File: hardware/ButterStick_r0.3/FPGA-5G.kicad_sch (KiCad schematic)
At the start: 1 part, among them U2 ECP5UM5G_85_CABGA381

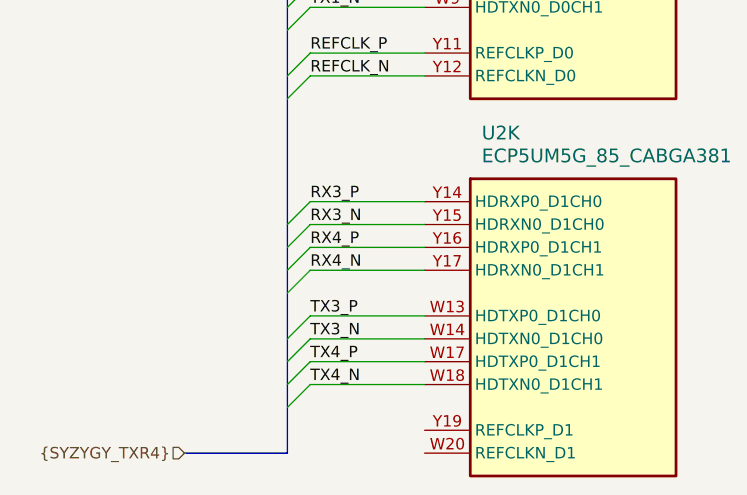
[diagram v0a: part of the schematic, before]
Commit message: hw.r0_3: routing improvements
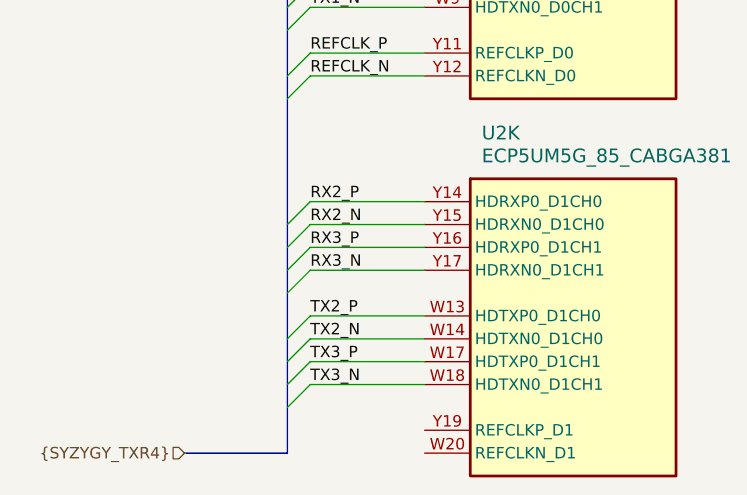
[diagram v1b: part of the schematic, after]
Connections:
- net RX4_N is gone; now on net RX3_N: U2.Y17 (HDRXN0_D1CH1)
- net RX4_P is gone; now on net RX3_P: U2.Y16 (HDRXP0_D1CH1)
- net TX4_N is gone; now on net TX3_N: U2.W18 (HDTXN0_D1CH1)
- net TX4_P is gone; now on net TX3_P: U2.W17 (HDTXP0_D1CH1)
- net RX3_N: no longer U2.Y15 (HDRXN0_D1CH0)
- net RX3_P: no longer U2.Y14 (HDRXP0_D1CH0)
- net TX3_N: no longer U2.W14 (HDTXN0_D1CH0)
- net TX3_P: no longer U2.W13 (HDTXP0_D1CH0)
- new net RX2_N: U2.Y15 (HDRXN0_D1CH0)
- new net RX2_P: U2.Y14 (HDRXP0_D1CH0)
- new net TX2_N: U2.W14 (HDTXN0_D1CH0)
- new net TX2_P: U2.W13 (HDTXP0_D1CH0)
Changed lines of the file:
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@@
 (kicad_sch (version 20200512) (host eeschema "5.99.0-unknown-c8476d6~101~ubuntu18.04.1")
-  (page 12 20)
+  (page 1 20)
   (paper "A4")
   (bus_entry (at 62.23 72.39) (size 2.54 -2.54))
@@
     (effects (font (size 1.27 1.27)) (justify left bottom))
   )
-  (label "RX3_P" (at 64.77 111.76 0)
+  (label "RX2_P" (at 64.77 111.76 0)
     (effects (font (size 1.27 1.27)) (justify left bottom))
   )
-  (label "RX3_N" (at 64.77 114.3 0)
+  (label "RX2_N" (at 64.77 114.3 0)
     (effects (font (size 1.27 1.27)) (justify left bottom))
   )
-  (label "RX4_P" (at 64.77 116.84 0)
+  (label "RX3_P" (at 64.77 116.84 0)
     (effects (font (size 1.27 1.27)) (justify left bottom))
   )
-  (label "RX4_N" (at 64.77 119.38 0)
+  (label "RX3_N" (at 64.77 119.38 0)
     (effects (font (size 1.27 1.27)) (justify left bottom))
   )
-  (label "TX3_P" (at 64.77 124.46 0)
+  (label "TX2_P" (at 64.77 124.46 0)
     (effects (font (size 1.27 1.27)) (justify left bottom))
   )
-  (label "TX3_N" (at 64.77 127 0)
+  (label "TX2_N" (at 64.77 127 0)
     (effects (font (size 1.27 1.27)) (justify left bottom))
   )
-  (label "TX4_P" (at 64.77 129.54 0)
+  (label "TX3_P" (at 64.77 129.54 0)
     (effects (font (size 1.27 1.27)) (justify left bottom))
   )
-  (label "TX4_N" (at 64.77 132.08 0)
+  (label "TX3_N" (at 64.77 132.08 0)
     (effects (font (size 1.27 1.27)) (justify left bottom))
   )

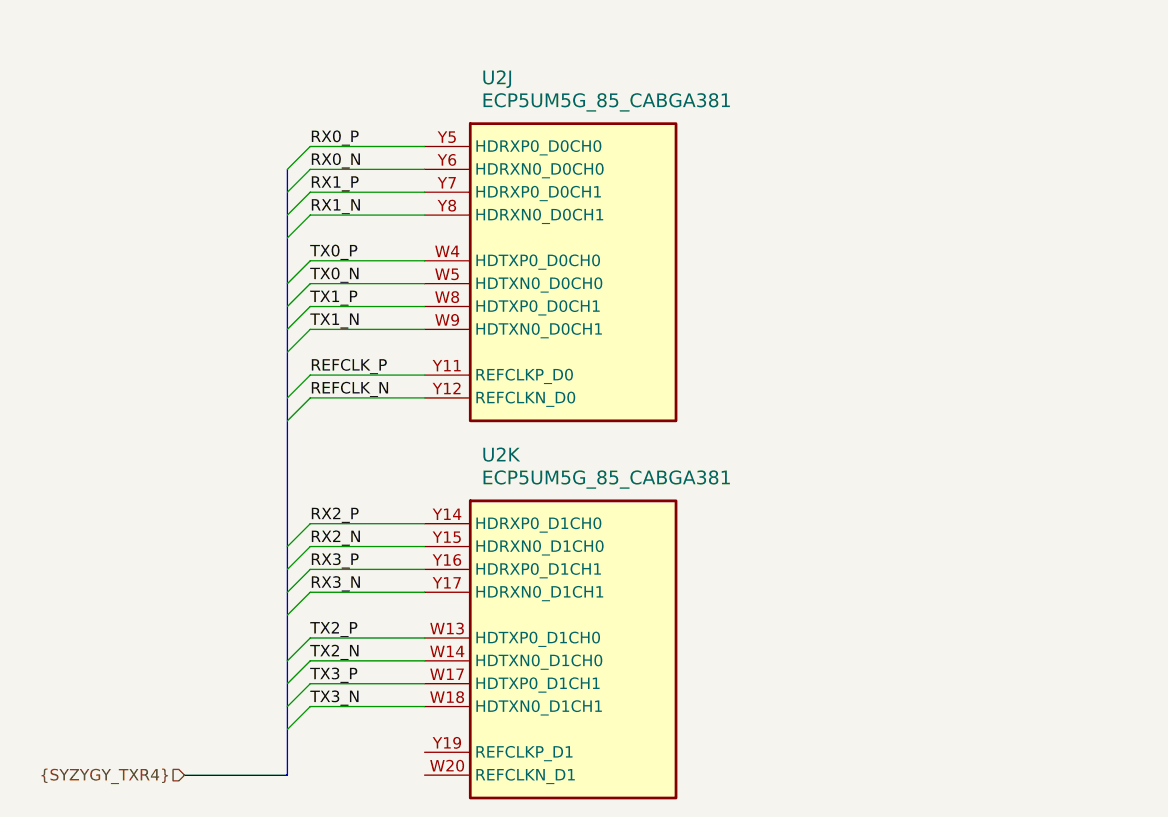
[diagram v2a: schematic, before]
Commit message: hw.r0_3: routed SYZYGY, begin routing RGMII/ULPI
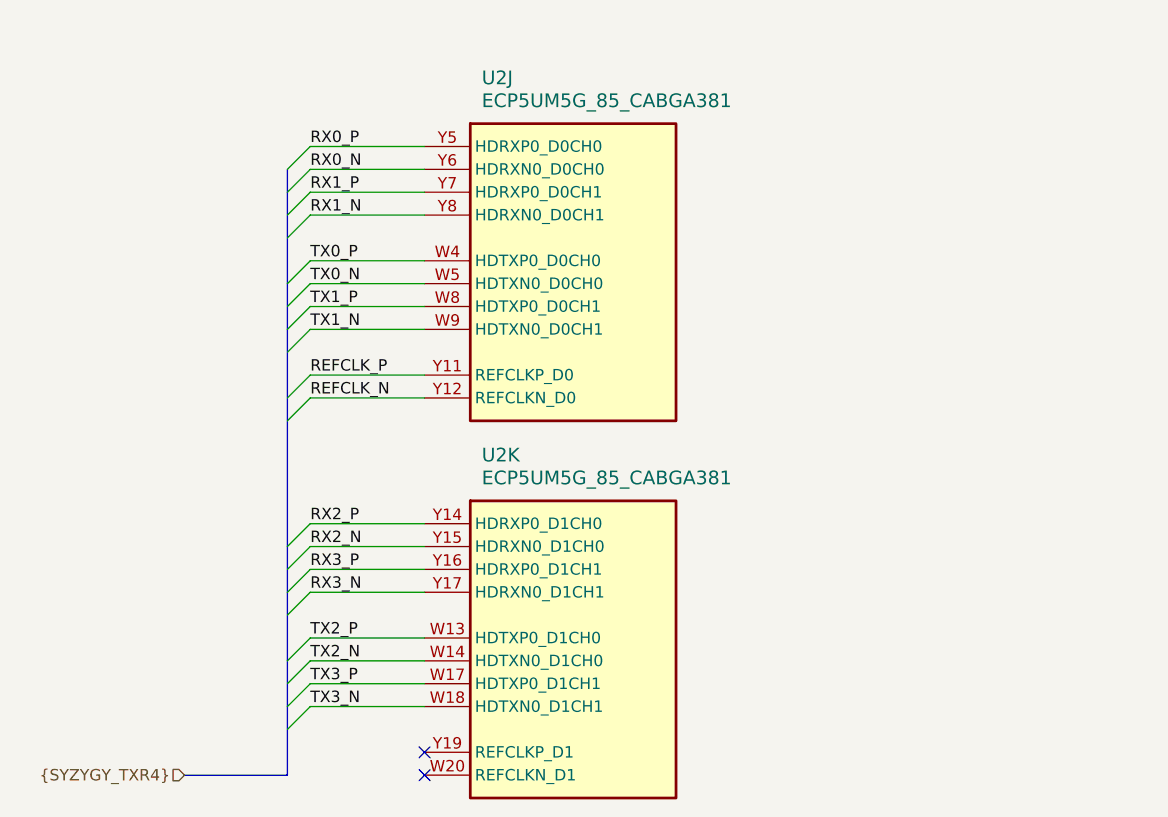
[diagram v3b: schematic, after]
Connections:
- no-connect marks 0 -> 2
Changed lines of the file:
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@@
 (kicad_sch (version 20200512) (host eeschema "5.99.0-unknown-711fc99~101~ubuntu18.04.1")
-  (page 1 20)
+  (page 11 19)
   (paper "A4")
+  (no_connect (at 77.47 137.16))
+  (no_connect (at 77.47 139.7))
   (bus_entry (at 62.23 72.39) (size 2.54 -2.54))
   (bus_entry (at 62.23 74.93) (size 2.54 -2.54))
@@
   (wire (pts (xy 77.47 132.08) (xy 64.77 132.08)))
   (bus (pts (xy 50.8 139.7) (xy 62.23 139.7)))
-  (bus (pts (xy 62.23 72.39) (xy 62.23 77.47)))
-  (bus (pts (xy 62.23 77.47) (xy 62.23 85.09)))
+  (bus (pts (xy 62.23 72.39) (xy 62.23 74.93)))
+  (bus (pts (xy 62.23 74.93) (xy 62.23 80.01)))
+  (bus (pts (xy 62.23 80.01) (xy 62.23 85.09)))
   (bus (pts (xy 62.23 85.09) (xy 62.23 90.17)))
   (bus (pts (xy 62.23 90.17) (xy 62.23 97.79)))

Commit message: hw.r0_3: major blocks roughly routed
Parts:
- renumbered U2 to U4
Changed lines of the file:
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@@
 (kicad_sch (version 20200512) (host eeschema "5.99.0-unknown-711fc99~101~ubuntu18.04.1")
-  (page 11 19)
+  (page 1 19)
   (paper "A4")
   (no_connect (at 77.47 137.16))
@@
   (bus (pts (xy 62.23 72.39) (xy 62.23 74.93)))
   (bus (pts (xy 62.23 74.93) (xy 62.23 80.01)))
-  (bus (pts (xy 62.23 80.01) (xy 62.23 85.09)))
-  (bus (pts (xy 62.23 85.09) (xy 62.23 90.17)))
-  (bus (pts (xy 62.23 90.17) (xy 62.23 97.79)))
-  (bus (pts (xy 62.23 97.79) (xy 62.23 114.3)))
-  (bus (pts (xy 62.23 114.3) (xy 62.23 119.38)))
-  (bus (pts (xy 62.23 119.38) (xy 62.23 127)))
-  (bus (pts (xy 62.23 127) (xy 62.23 132.08)))
-  (bus (pts (xy 62.23 132.08) (xy 62.23 139.7)))
+  (bus (pts (xy 62.23 80.01) (xy 62.23 87.63)))
+  (bus (pts (xy 62.23 87.63) (xy 62.23 92.71)))
+  (bus (pts (xy 62.23 92.71) (xy 62.23 100.33)))
+  (bus (pts (xy 62.23 100.33) (xy 62.23 116.84)))
+  (bus (pts (xy 62.23 116.84) (xy 62.23 121.92)))
+  (bus (pts (xy 62.23 121.92) (xy 62.23 129.54)))
+  (bus (pts (xy 62.23 129.54) (xy 62.23 134.62)))
+  (bus (pts (xy 62.23 134.62) (xy 62.23 139.7)))
   (label "RX0_P" (at 64.77 69.85 0)
     (effects (font (size 1.27 1.27)) (justify left bottom))
@@
   )
   (symbol (lib_id "gkl_lattice:ECP5UM5G_85_CABGA381") (at 77.47 72.39 0) (unit 10)
-    (property "Reference" "U2" (id 0) (at 83.82 62.23 0)
+    (property "Reference" "U4" (id 0) (at 83.82 62.23 0)
       (effects (font (size 1.524 1.524)) (justify left))
     )
@@
   )
   (symbol (lib_id "gkl_lattice:ECP5UM5G_85_CABGA381") (at 77.47 114.3 0) (unit 11)
-    (property "Reference" "U2" (id 0) (at 83.82 104.14 0)
+    (property "Reference" "U4" (id 0) (at 83.82 104.14 0)
       (effects (font (size 1.524 1.524)) (justify left))
     )

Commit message: hw.r0d3: complete first pass of routing
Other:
- moved on the sheet: U4J, U4K

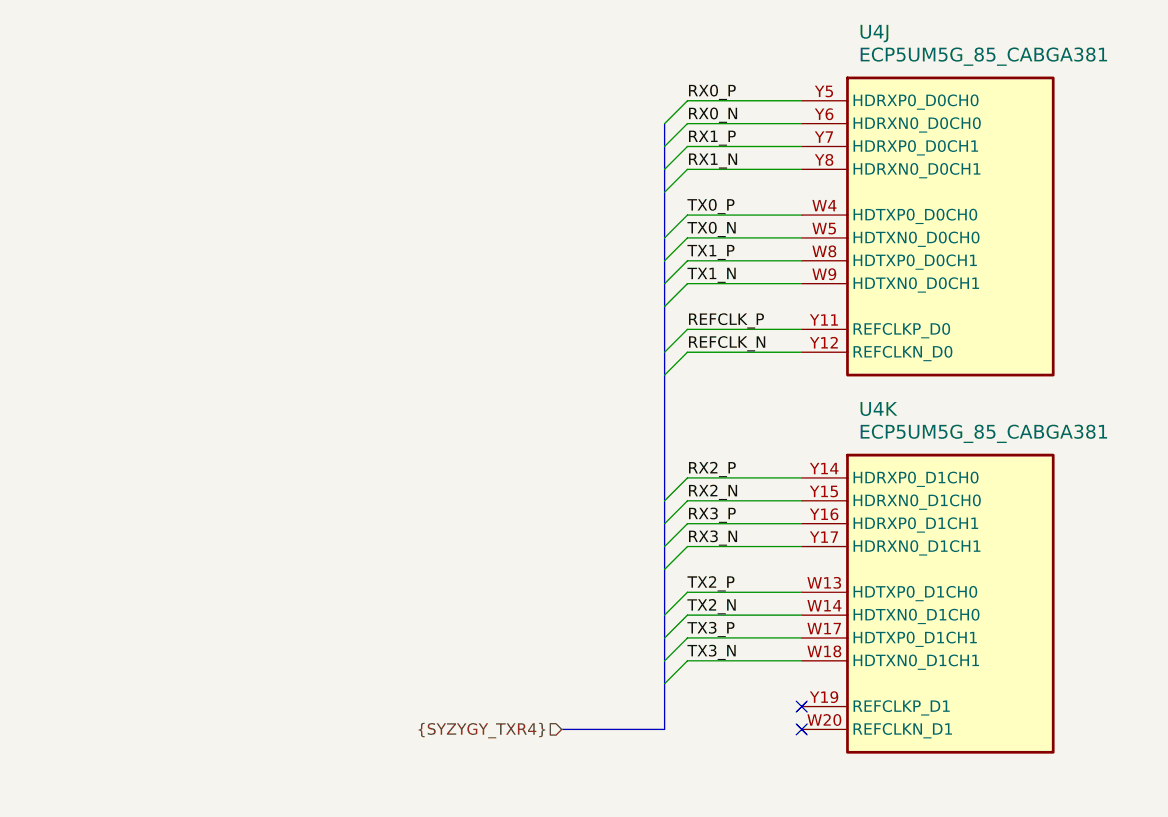
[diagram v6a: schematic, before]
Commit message: hw.r0d3: Updated all DCDC supplies Added serdes power supplies
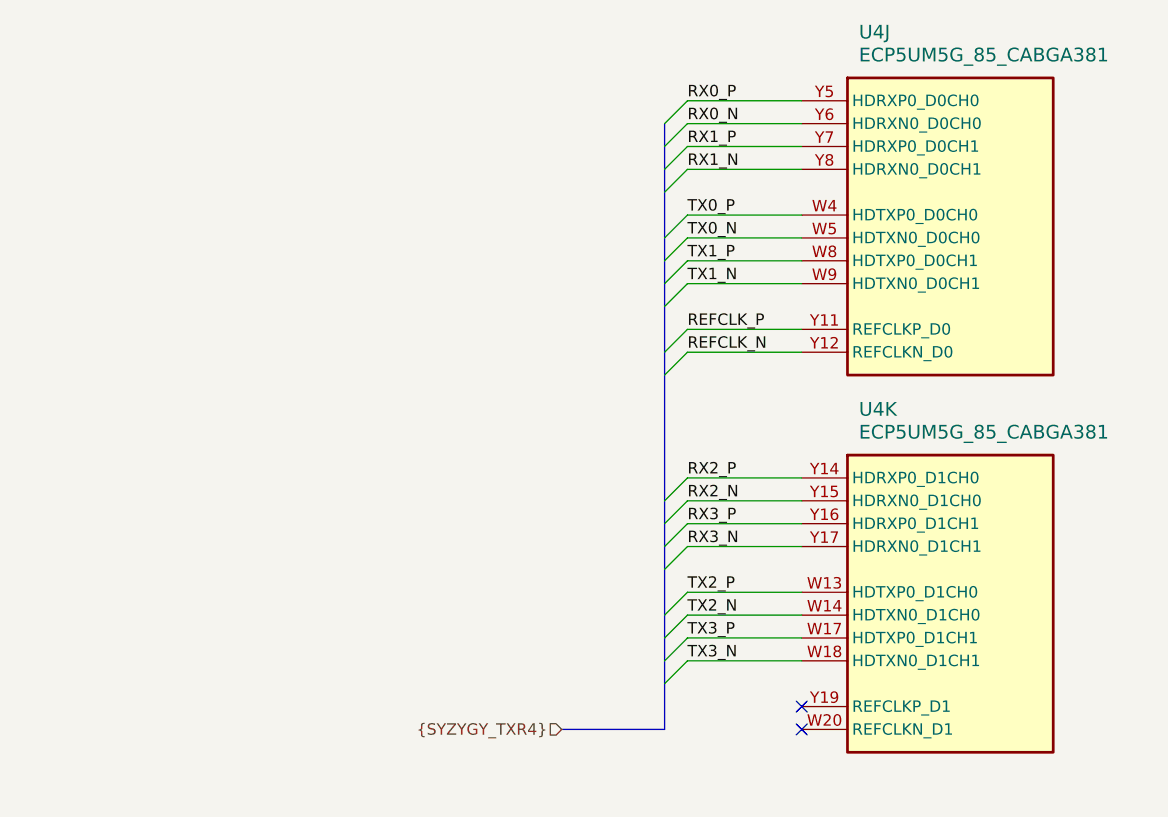
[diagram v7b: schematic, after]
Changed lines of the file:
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@@
-(kicad_sch (version 20200618) (host eeschema "5.99.0-unknown-476558e~101~ubuntu18.04.1")
+(kicad_sch (version 20200618) (host eeschema "5.99.0-unknown-73168a9~101~ubuntu18.04.1")
   (page 1 19)
   (paper "A4")
@@
     (stroke (width 0) (type solid) (color 0 0 0 0))
   )
-  (bus (pts (xy 104.14 85.09) (xy 104.14 87.63))
+  (bus (pts (xy 104.14 85.09) (xy 104.14 92.71))
     (stroke (width 0) (type solid) (color 0 0 0 0))
   )
-  (bus (pts (xy 104.14 87.63) (xy 104.14 95.25))
+  (bus (pts (xy 104.14 92.71) (xy 104.14 109.22))
     (stroke (width 0) (type solid) (color 0 0 0 0))
   )
-  (bus (pts (xy 104.14 95.25) (xy 104.14 111.76))
+  (bus (pts (xy 104.14 109.22) (xy 104.14 114.3))
     (stroke (width 0) (type solid) (color 0 0 0 0))
   )
-  (bus (pts (xy 104.14 111.76) (xy 104.14 116.84))
+  (bus (pts (xy 104.14 114.3) (xy 104.14 121.92))
     (stroke (width 0) (type solid) (color 0 0 0 0))
   )
-  (bus (pts (xy 104.14 116.84) (xy 104.14 124.46))
+  (bus (pts (xy 104.14 121.92) (xy 104.14 124.46))
     (stroke (width 0) (type solid) (color 0 0 0 0))
   )
-  (bus (pts (xy 104.14 124.46) (xy 104.14 127))
+  (bus (pts (xy 104.14 124.46) (xy 104.14 129.54))
     (stroke (width 0) (type solid) (color 0 0 0 0))
   )
-  (bus (pts (xy 104.14 127) (xy 104.14 134.62))
+  (bus (pts (xy 104.14 129.54) (xy 104.14 134.62))
     (stroke (width 0) (type solid) (color 0 0 0 0))
   )

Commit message: hw.r0d3: Tweaking routing
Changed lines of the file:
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@@
 (kicad_sch (version 20200618) (host eeschema "5.99.0-unknown-73168a9~101~ubuntu18.04.1")
-  (page 1 19)
+  (page 11 19)
   (paper "A4")
   (no_connect (at 119.38 132.08))
@@
     (stroke (width 0) (type solid) (color 0 0 0 0))
   )
-  (bus (pts (xy 104.14 85.09) (xy 104.14 92.71))
+  (bus (pts (xy 104.14 85.09) (xy 104.14 87.63))
     (stroke (width 0) (type solid) (color 0 0 0 0))
   )
-  (bus (pts (xy 104.14 92.71) (xy 104.14 109.22))
+  (bus (pts (xy 104.14 87.63) (xy 104.14 95.25))
     (stroke (width 0) (type solid) (color 0 0 0 0))
   )
-  (bus (pts (xy 104.14 109.22) (xy 104.14 114.3))
+  (bus (pts (xy 104.14 95.25) (xy 104.14 111.76))
     (stroke (width 0) (type solid) (color 0 0 0 0))
   )
-  (bus (pts (xy 104.14 114.3) (xy 104.14 121.92))
+  (bus (pts (xy 104.14 111.76) (xy 104.14 116.84))
     (stroke (width 0) (type solid) (color 0 0 0 0))
   )
-  (bus (pts (xy 104.14 121.92) (xy 104.14 124.46))
+  (bus (pts (xy 104.14 116.84) (xy 104.14 124.46))
     (stroke (width 0) (type solid) (color 0 0 0 0))
   )
-  (bus (pts (xy 104.14 124.46) (xy 104.14 129.54))
+  (bus (pts (xy 104.14 124.46) (xy 104.14 127))
     (stroke (width 0) (type solid) (color 0 0 0 0))
   )
-  (bus (pts (xy 104.14 129.54) (xy 104.14 134.62))
+  (bus (pts (xy 104.14 127) (xy 104.14 134.62))
     (stroke (width 0) (type solid) (color 0 0 0 0))
   )
